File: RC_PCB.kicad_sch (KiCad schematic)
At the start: 23 parts, among them SW1 SW_Push, SW2 SW_Push, SW3 SW_Push, SW4 SW_Push, U1 RFM9x, U2 Teensy4.0, U3 128x64_OLED, U4 Joystick, U5 Joystick

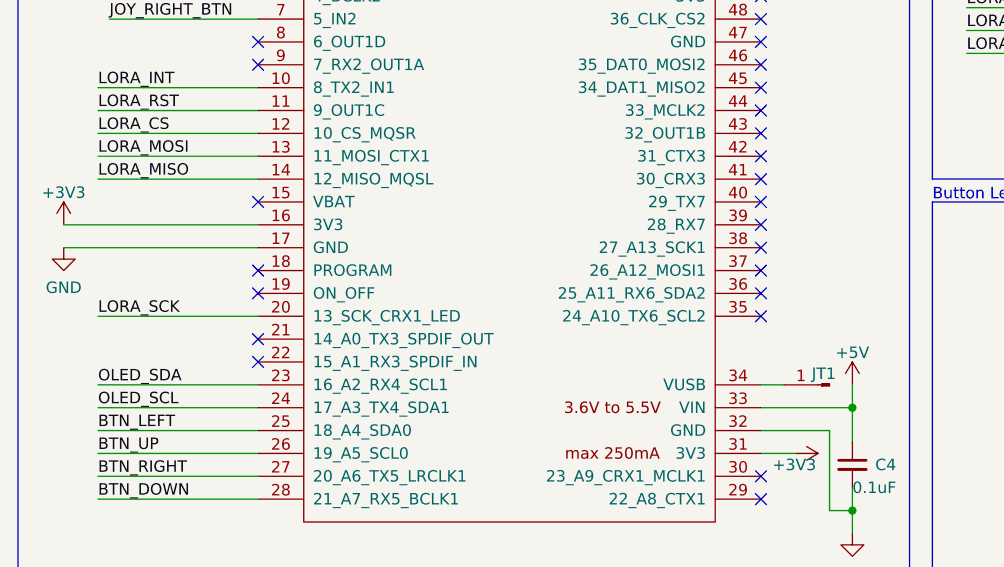
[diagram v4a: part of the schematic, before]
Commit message: updated oled footprint
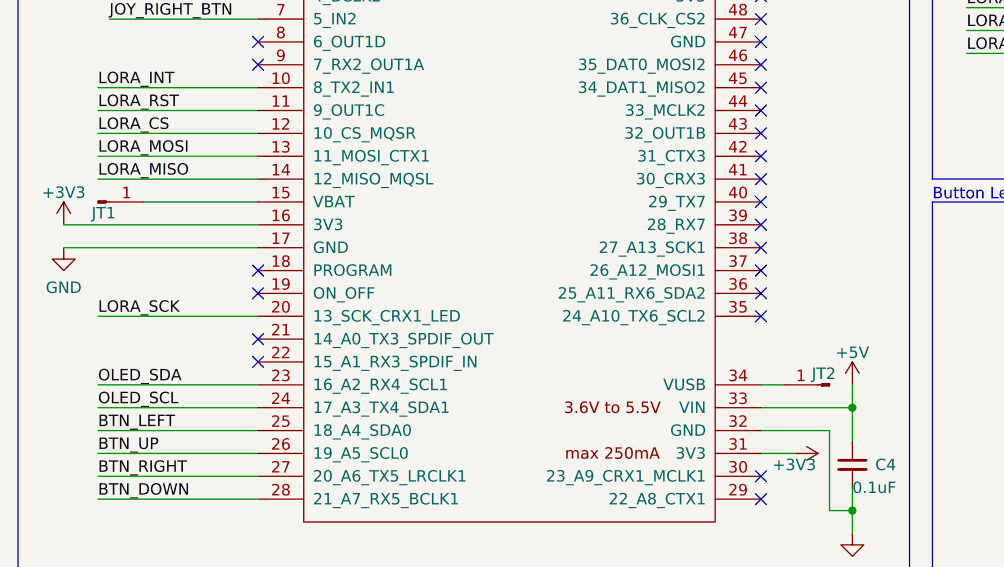
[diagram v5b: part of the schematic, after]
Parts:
- added JT1: Conn_01x01_Male, Connector_PinHeader_2.54mm:PinHeader_1x01_P2.54mm_Vertical, symbol Connector:Conn_01x01_Male
- renumbered JT1 to JT2
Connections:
- net at U2.15 (VBAT): now also JT1.1 (Pin_1)
- no-connect marks 39 -> 38
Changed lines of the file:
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@@
   (no_connect (at 97.79 48.26))
   (no_connect (at 97.79 93.98))
-  (no_connect (at 41.91 60.96))
   (no_connect (at 41.91 43.18))
   (no_connect (at 41.91 45.72))
@@
     (stroke (width 0) (type default) (color 0 0 0 0))
   )
+  (wire (pts (xy 29.21 60.96) (xy 41.91 60.96))
+    (stroke (width 0) (type default) (color 0 0 0 0))
+  )
   (wire (pts (xy 69.85 176.53) (xy 69.85 181.61))
     (stroke (width 0) (type default) (color 0 0 0 0))
@@
     )
     (property "Datasheet" "" (id 3) (at 154.94 116.84 0)
+      (effects (font (size 1.27 1.27)) hide)
+    )
+    (pin "1")
+  )
+  (symbol (lib_id "Connector:Conn_01x01_Male") (at 24.13 60.96 0) (unit 1)
+    (in_bom yes) (on_board yes)
+    (property "Reference" "JT1" (id 0) (at 24.765 62.199 0))
+    (property "Value" "Conn_01x01_Male" (id 1) (at 24.765 62.1991 0)
+      (effects (font (size 1.27 1.27)) hide)
+    )
+    (property "Footprint" "Connector_PinHeader_2.54mm:PinHeader_1x01_P2.54mm_Vertical" (id 2) (at 24.13 60.96 0)
+      (effects (font (size 1.27 1.27)) hide)
+    )
+    (property "Datasheet" "~" (id 3) (at 24.13 60.96 0)
       (effects (font (size 1.27 1.27)) hide)
     )
@@
   (symbol (lib_id "Connector:Conn_01x01_Male") (at 105.41 81.28 180) (unit 1)
     (in_bom yes) (on_board yes)
-    (property "Reference" "JT1" (id 0) (at 104.775 80.041 0))
+    (property "Reference" "JT2" (id 0) (at 104.775 80.041 0))
     (property "Value" "Conn_01x01_Male" (id 1) (at 104.775 80.0409 0)
       (effects (font (size 1.27 1.27)) hide)
@@
       (reference "C7") (unit 1) (value "0.1uF") (footprint "Capacitor_SMD:C_0805_2012Metric_Pad1.18x1.45mm_HandSolder")
     )
+    (path "/1c4dcaec-bb0d-4e4b-938d-418142c896e7"
+      (reference "JT1") (unit 1) (value "Conn_01x01_Male") (footprint "Connector_PinHeader_2.54mm:PinHeader_1x01_P2.54mm_Vertical")
+    )
     (path "/bbd6cdc6-f9a9-4877-a26f-754919f9430f"
-      (reference "JT1") (unit 1) (value "Conn_01x01_Male") (footprint "Connector_PinHeader_2.54mm:PinHeader_1x01_P2.54mm_Vertical")
+      (reference "JT2") (unit 1) (value "Conn_01x01_Male") (footprint "Connector_PinHeader_2.54mm:PinHeader_1x01_P2.54mm_Vertical")
     )
     (path "/3bf5c161-bb82-4c3f-a7d3-0e5786e299da"
